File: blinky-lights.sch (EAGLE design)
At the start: 20 parts, among them Q1 N3, U1 555, U2 A2678EAT

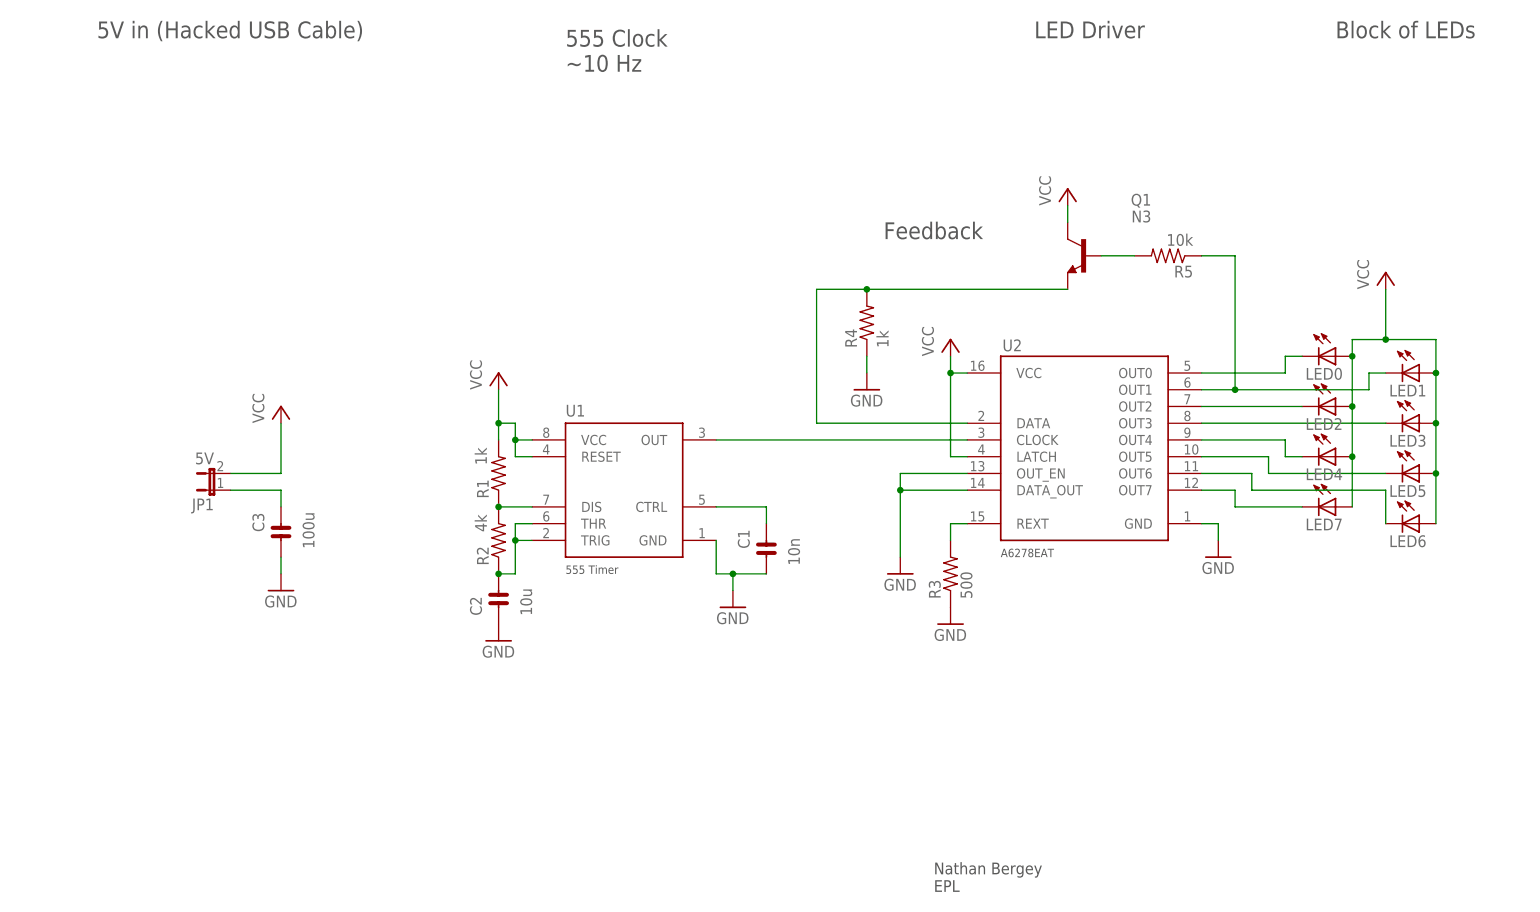
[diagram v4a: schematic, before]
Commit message: replaced transistor with a fet
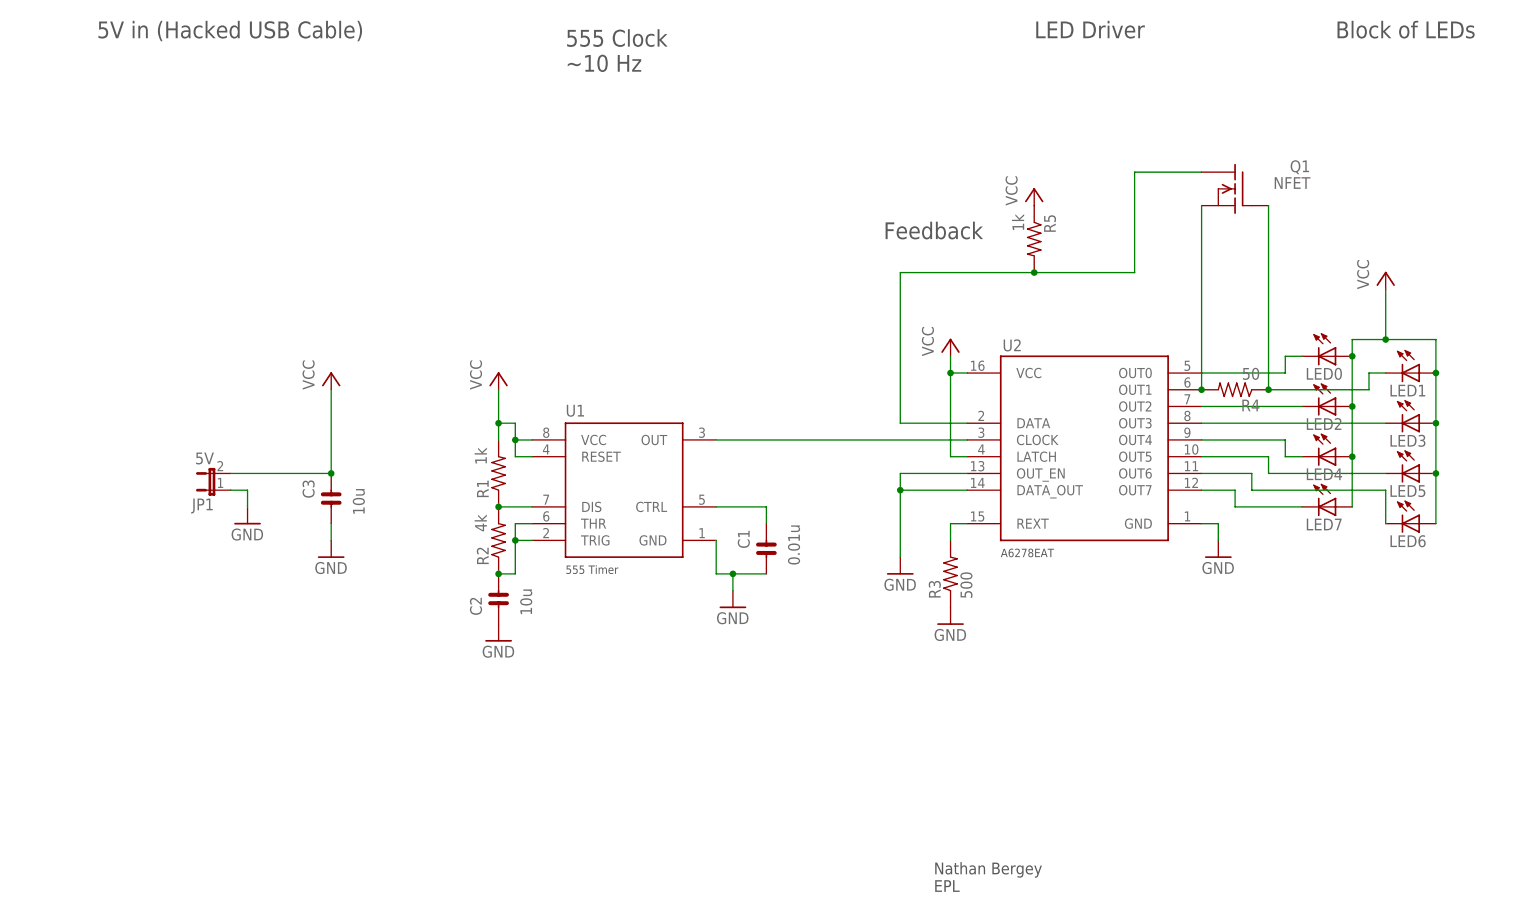
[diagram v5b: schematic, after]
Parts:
- C1: value 10n -> 0.01u
- C3: value 100u -> 10u
- LED0, LED1, LED2, LED3, LED4, LED5, LED6, LED7: device led:LED5MM -> led:LED3MM
- Q1: value N3 -> NFET; device blinky-lights:N3 -> blinky-lights:NFET
- R4: value 1k -> 50
- R5: value 10k -> 1k
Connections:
- removed net DATA: Q1.E, R4.2, U2.DATA
- removed net N$12: Q1.B, R5.2
- removed net N$13: C3.A, JP1.1
- new net N$5: Q1.S, R4.2, U2.OUT1
- net FEEDBACK: now also Q1.D, Q1.G, R4.1, R5.2, U2.DATA; no longer R5.1, U2.OUT1
- net GND: now also JP1.1; no longer R4.1
- net VCC: now also C3.A, R5.1; no longer Q1.C
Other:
- moved on the sheet: C3, Q1, R4, R5
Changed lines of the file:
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@@
 <part name="U1" library="blinky-lights" deviceset="555" device=""/>
 <part name="U2" library="blinky-lights" deviceset="A2678EAT" device=""/>
-<part name="LED0" library="led" deviceset="LED" device="5MM"/>
-<part name="LED2" library="led" deviceset="LED" device="5MM"/>
-<part name="LED4" library="led" deviceset="LED" device="5MM"/>
-<part name="LED7" library="led" deviceset="LED" device="5MM"/>
-<part name="LED1" library="led" deviceset="LED" device="5MM"/>
-<part name="LED3" library="led" deviceset="LED" device="5MM"/>
-<part name="LED5" library="led" deviceset="LED" device="5MM"/>
-<part name="LED6" library="led" deviceset="LED" device="5MM"/>
+<part name="LED0" library="led" deviceset="LED" device="3MM"/>
+<part name="LED2" library="led" deviceset="LED" device="3MM"/>
+<part name="LED4" library="led" deviceset="LED" device="3MM"/>
+<part name="LED7" library="led" deviceset="LED" device="3MM"/>
+<part name="LED1" library="led" deviceset="LED" device="3MM"/>
+<part name="LED3" library="led" deviceset="LED" device="3MM"/>
+<part name="LED5" library="led" deviceset="LED" device="3MM"/>
+<part name="LED6" library="led" deviceset="LED" device="3MM"/>
 <part name="P+1" library="supply1" deviceset="VCC" device=""/>
 <part name="P+2" library="supply1" deviceset="VCC" device=""/>
@@
 <part name="FRAME1" library="frames" deviceset="LETTER_L" device="" value="0.1"/>
 <part name="JP1" library="jumper" deviceset="JP1E" device="" value="5V"/>
-<part name="C1" library="blinky-lights" deviceset="CAP" device="" value="10n"/>
+<part name="C1" library="blinky-lights" deviceset="CAP" device="" value="0.01u"/>
 <part name="C2" library="blinky-lights" deviceset="CAP" device="" value="10u"/>
 <part name="GND6" library="supply1" deviceset="GND" device=""/>
 <part name="GND2" library="supply1" deviceset="GND" device=""/>
-<part name="Q1" library="blinky-lights" deviceset="N3*" device=""/>
-<part name="R4" library="rcl" deviceset="R-US_" device="VMTB60" value="1k"/>
-<part name="GND7" library="supply1" deviceset="GND" device=""/>
+<part name="C3" library="blinky-lights" deviceset="CAP" device="" value="10u"/>
+<part name="Q1" library="blinky-lights" deviceset="NFET" device=""/>
+<part name="GND8" library="supply1" deviceset="GND" device=""/>
+<part name="R4" library="rcl" deviceset="R-US_" device="VMTB60" value="50"/>
+<part name="R5" library="rcl" deviceset="R-US_" device="VMTB60" value="1k"/>
 <part name="P+5" library="supply1" deviceset="VCC" device=""/>
-<part name="R5" library="rcl" deviceset="R-US_" device="VMTB60" value="10k"/>
-<part name="C3" library="blinky-lights" deviceset="CAP" device="" value="100u"/>
 </parts>
 <sheets>
@@
 <instance part="P+2" gate="VCC" x="152.4" y="111.76"/>
 <instance part="P+3" gate="VCC" x="83.82" y="106.68"/>
-<instance part="P+4" gate="VCC" x="50.8" y="101.6"/>
+<instance part="P+4" gate="VCC" x="58.42" y="106.68"/>
 <instance part="GND1" gate="1" x="193.04" y="78.74"/>
-<instance part="GND3" gate="1" x="50.8" y="73.66"/>
+<instance part="GND3" gate="1" x="45.72" y="83.82"/>
 <instance part="R3" gate="G$1" x="152.4" y="76.2" rot="R90"/>
 <instance part="R1" gate="G$1" x="83.82" y="91.44" smashed="yes" rot="R90">
@@
 <instance part="GND6" gate="1" x="83.82" y="66.04"/>
 <instance part="GND2" gate="1" x="119.38" y="71.12"/>
-<instance part="Q1" gate="G$1" x="172.72" y="124.46" rot="MR0"/>
-<instance part="R4" gate="G$1" x="139.7" y="114.3" rot="R90"/>
-<instance part="GND7" gate="1" x="139.7" y="104.14"/>
-<instance part="P+5" gate="VCC" x="170.18" y="134.62"/>
-<instance part="R5" gate="G$1" x="185.42" y="124.46" rot="R180"/>
-<instance part="C3" gate="G$1" x="50.8" y="81.28" smashed="yes">
-<attribute name="NAME" x="48.26" y="82.55" size="1.778" layer="95" rot="R90"/>
-<attribute name="VALUE" x="55.88" y="80.01" size="1.778" layer="96" rot="R90"/>
-</instance>
+<instance part="C3" gate="G$1" x="58.42" y="86.36" smashed="yes">
+<attribute name="NAME" x="55.88" y="87.63" size="1.778" layer="95" rot="R90"/>
+<attribute name="VALUE" x="63.5" y="85.09" size="1.778" layer="96" rot="R90"/>
+</instance>
+<instance part="Q1" gate="G$1" x="195.58" y="134.62" rot="MR0"/>
+<instance part="GND8" gate="1" x="58.42" y="78.74"/>
+<instance part="R4" gate="G$1" x="195.58" y="104.14" rot="R180"/>
+<instance part="R5" gate="G$1" x="165.1" y="127" rot="R270"/>
+<instance part="P+5" gate="VCC" x="165.1" y="134.62"/>
 </instances>
 <busses>
@@
 <wire x1="218.44" y1="106.68" x2="215.9" y2="106.68" width="0.1524" layer="91"/>
 <wire x1="215.9" y1="106.68" x2="215.9" y2="104.14" width="0.1524" layer="91"/>
-<pinref part="U2" gate="G$1" pin="OUT1"/>
-<wire x1="215.9" y1="104.14" x2="195.58" y2="104.14" width="0.1524" layer="91"/>
-<wire x1="195.58" y1="104.14" x2="190.5" y2="104.14" width="0.1524" layer="91"/>
-<wire x1="195.58" y1="104.14" x2="195.58" y2="124.46" width="0.1524" layer="91"/>
-<junction x="195.58" y="104.14"/>
-<pinref part="R5" gate="G$1" pin="1"/>
-<wire x1="190.5" y1="124.46" x2="195.58" y2="124.46" width="0.1524" layer="91"/>
+<pinref part="R4" gate="G$1" pin="1"/>
+<wire x1="200.66" y1="104.14" x2="215.9" y2="104.14" width="0.1524" layer="91"/>
+<wire x1="200.66" y1="104.14" x2="200.66" y2="132.08" width="0.1524" layer="91"/>
+<junction x="200.66" y="104.14"/>
+<pinref part="Q1" gate="G$1" pin="G"/>
+</segment>
+<segment>
+<pinref part="U2" gate="G$1" pin="DATA"/>
+<wire x1="154.94" y1="99.06" x2="144.78" y2="99.06" width="0.1524" layer="91"/>
+<wire x1="144.78" y1="99.06" x2="144.78" y2="121.92" width="0.1524" layer="91"/>
+<pinref part="R5" gate="G$1" pin="2"/>
+<wire x1="144.78" y1="121.92" x2="165.1" y2="121.92" width="0.1524" layer="91"/>
+<wire x1="165.1" y1="121.92" x2="180.34" y2="121.92" width="0.1524" layer="91"/>
+<wire x1="180.34" y1="121.92" x2="180.34" y2="137.16" width="0.1524" layer="91"/>
+<junction x="165.1" y="121.92"/>
+<pinref part="Q1" gate="G$1" pin="D"/>
+<wire x1="180.34" y1="137.16" x2="190.5" y2="137.16" width="0.1524" layer="91"/>
 </segment>
 </net>
@@
 </segment>
 <segment>
+<pinref part="C3" gate="G$1" pin="A"/>
+<pinref part="P+4" gate="VCC" pin="VCC"/>
+<wire x1="58.42" y1="91.44" x2="58.42" y2="104.14" width="0.1524" layer="91"/>
 <pinref part="JP1" gate="A" pin="2"/>
-<pinref part="P+4" gate="VCC" pin="VCC"/>
-<wire x1="43.18" y1="91.44" x2="50.8" y2="91.44" width="0.1524" layer="91"/>
-<wire x1="50.8" y1="91.44" x2="50.8" y2="99.06" width="0.1524" layer="91"/>
-</segment>
-<segment>
-<pinref part="Q1" gate="G$1" pin="C"/>
+<wire x1="43.18" y1="91.44" x2="58.42" y2="91.44" width="0.1524" layer="91"/>
+<junction x="58.42" y="91.44"/>
+</segment>
+<segment>
+<pinref part="R5" gate="G$1" pin="1"/>
 <pinref part="P+5" gate="VCC" pin="VCC"/>
-<wire x1="170.18" y1="129.54" x2="170.18" y2="132.08" width="0.1524" layer="91"/>
 </segment>
 </net>
@@
 </segment>
 <segment>
-<pinref part="R4" gate="G$1" pin="1"/>
-<pinref part="GND7" gate="1" pin="GND"/>
-<wire x1="139.7" y1="106.68" x2="139.7" y2="109.22" width="0.1524" layer="91"/>
+<pinref part="JP1" gate="A" pin="1"/>
+<pinref part="GND3" gate="1" pin="GND"/>
+<wire x1="43.18" y1="88.9" x2="45.72" y2="88.9" width="0.1524" layer="91"/>
+<wire x1="45.72" y1="88.9" x2="45.72" y2="86.36" width="0.1524" layer="91"/>
 </segment>
 <segment>
 <pinref part="C3" gate="G$1" pin="C"/>
-<pinref part="GND3" gate="1" pin="GND"/>
-<wire x1="50.8" y1="78.74" x2="50.8" y2="76.2" width="0.1524" layer="91"/>
+<pinref part="GND8" gate="1" pin="GND"/>
+<wire x1="58.42" y1="81.28" x2="58.42" y2="83.82" width="0.1524" layer="91"/>
 </segment>
 </net>
@@
 </segment>
 </net>
-<net name="DATA" class="0">
-<segment>
-<wire x1="139.7" y1="119.38" x2="132.08" y2="119.38" width="0.1524" layer="91"/>
-<wire x1="132.08" y1="119.38" x2="132.08" y2="99.06" width="0.1524" layer="91"/>
-<pinref part="U2" gate="G$1" pin="DATA"/>
-<wire x1="132.08" y1="99.06" x2="154.94" y2="99.06" width="0.1524" layer="91"/>
+<net name="N$5" class="0">
+<segment>
+<pinref part="U2" gate="G$1" pin="OUT1"/>
 <pinref part="R4" gate="G$1" pin="2"/>
-<pinref part="Q1" gate="G$1" pin="E"/>
-<wire x1="170.18" y1="119.38" x2="139.7" y2="119.38" width="0.1524" layer="91"/>
-<junction x="139.7" y="119.38"/>
-</segment>
-</net>
-<net name="N$12" class="0">
-<segment>
-<pinref part="R5" gate="G$1" pin="2"/>
-<pinref part="Q1" gate="G$1" pin="B"/>
-<wire x1="180.34" y1="124.46" x2="175.26" y2="124.46" width="0.1524" layer="91"/>
-</segment>
-</net>
-<net name="N$13" class="0">
-<segment>
-<pinref part="JP1" gate="A" pin="1"/>
-<wire x1="43.18" y1="88.9" x2="50.8" y2="88.9" width="0.1524" layer="91"/>
-<pinref part="C3" gate="G$1" pin="A"/>
-<wire x1="50.8" y1="88.9" x2="50.8" y2="86.36" width="0.1524" layer="91"/>
-</segment>
-</net>
+<pinref part="Q1" gate="G$1" pin="S"/>
+<wire x1="190.5" y1="132.08" x2="190.5" y2="104.14" width="0.1524" layer="91"/>
+<junction x="190.5" y="104.14"/>
+</segment>
+</net>

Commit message: board layout
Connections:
- new net SENSE: LED1.C, Q1.G, R4.1
- net FEEDBACK: no longer LED1.C, Q1.G, R4.1
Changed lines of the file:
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@@
 <net name="FEEDBACK" class="0">
-<segment>
-<pinref part="LED1" gate="G$1" pin="C"/>
-<wire x1="218.44" y1="106.68" x2="215.9" y2="106.68" width="0.1524" layer="91"/>
-<wire x1="215.9" y1="106.68" x2="215.9" y2="104.14" width="0.1524" layer="91"/>
-<pinref part="R4" gate="G$1" pin="1"/>
-<wire x1="200.66" y1="104.14" x2="215.9" y2="104.14" width="0.1524" layer="91"/>
-<wire x1="200.66" y1="104.14" x2="200.66" y2="132.08" width="0.1524" layer="91"/>
-<junction x="200.66" y="104.14"/>
-<pinref part="Q1" gate="G$1" pin="G"/>
-</segment>
 <segment>
 <pinref part="U2" gate="G$1" pin="DATA"/>
@@
 </segment>
 </net>
+<net name="SENSE" class="0">
+<segment>
+<pinref part="LED1" gate="G$1" pin="C"/>
+<wire x1="218.44" y1="106.68" x2="215.9" y2="106.68" width="0.1524" layer="91"/>
+<wire x1="215.9" y1="106.68" x2="215.9" y2="104.14" width="0.1524" layer="91"/>
+<pinref part="R4" gate="G$1" pin="1"/>
+<wire x1="200.66" y1="104.14" x2="215.9" y2="104.14" width="0.1524" layer="91"/>
+<wire x1="200.66" y1="104.14" x2="200.66" y2="132.08" width="0.1524" layer="91"/>
+<junction x="200.66" y="104.14"/>
+<pinref part="Q1" gate="G$1" pin="G"/>
+</segment>
+</net>
 </nets>
 </sheet>
 </sheets>
+<errors>
+</errors>
 </schematic>
 </drawing>

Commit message: schematic and board clean up
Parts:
- R4: value 50 -> 10
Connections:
- net SENSE: no longer Q1.G
- net VCC: now also Q1.G
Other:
- note added: "555 In Astable Mode ~10 Hz"
- note added: "LED Driver/Shift Register"
- note removed: "555 Clock ~10 Hz"
- note removed: "Feedback"
- note removed: "LED Driver"
- moved on the sheet: C1, C2, C3, JP1, LED0, LED1, LED2, LED3, LED4, LED5, LED6, LED7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

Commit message: board clean up, got rid of last airwire
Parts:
- LED0, LED1, LED2, LED3, LED4, LED5, LED6, LED7: value (none) -> LED3MM; device led:LED3MM -> blinky-lights:LED3MM
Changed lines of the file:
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@@
 <part name="U1" library="blinky-lights" deviceset="555" device=""/>
 <part name="U2" library="blinky-lights" deviceset="A2678EAT" device=""/>
-<part name="LED0" library="led" deviceset="LED" device="3MM"/>
-<part name="LED2" library="led" deviceset="LED" device="3MM"/>
-<part name="LED4" library="led" deviceset="LED" device="3MM"/>
-<part name="LED7" library="led" deviceset="LED" device="3MM"/>
-<part name="LED1" library="led" deviceset="LED" device="3MM"/>
-<part name="LED3" library="led" deviceset="LED" device="3MM"/>
-<part name="LED5" library="led" deviceset="LED" device="3MM"/>
-<part name="LED6" library="led" deviceset="LED" device="3MM"/>
+<part name="LED0" library="blinky-lights" deviceset="LED3MM" device=""/>
+<part name="LED2" library="blinky-lights" deviceset="LED3MM" device=""/>
+<part name="LED4" library="blinky-lights" deviceset="LED3MM" device=""/>
+<part name="LED7" library="blinky-lights" deviceset="LED3MM" device=""/>
+<part name="LED1" library="blinky-lights" deviceset="LED3MM" device=""/>
+<part name="LED3" library="blinky-lights" deviceset="LED3MM" device=""/>
+<part name="LED5" library="blinky-lights" deviceset="LED3MM" device=""/>
+<part name="LED6" library="blinky-lights" deviceset="LED3MM" device=""/>
 <part name="P+1" library="supply1" deviceset="VCC" device=""/>
 <part name="P+2" library="supply1" deviceset="VCC" device=""/>
@@
 <instance part="U1" gate="G$1" x="88.9" y="93.98"/>
 <instance part="U2" gate="G$1" x="162.56" y="99.06"/>
-<instance part="LED0" gate="G$1" x="210.82" y="114.3" rot="R270"/>
-<instance part="LED2" gate="G$1" x="210.82" y="106.68" rot="R270"/>
-<instance part="LED4" gate="G$1" x="210.82" y="99.06" rot="R270"/>
-<instance part="LED7" gate="G$1" x="210.82" y="91.44" rot="R270"/>
-<instance part="LED1" gate="G$1" x="223.52" y="111.76" rot="R270"/>
-<instance part="LED3" gate="G$1" x="223.52" y="104.14" rot="R270"/>
-<instance part="LED5" gate="G$1" x="223.52" y="96.52" rot="R270"/>
-<instance part="LED6" gate="G$1" x="223.52" y="88.9" rot="R270"/>
+<instance part="LED0" gate="G$1" x="210.82" y="114.3" smashed="yes" rot="R270">
+<attribute name="NAME" x="206.248" y="110.744" size="1.778" layer="95"/>
+</instance>
+<instance part="LED2" gate="G$1" x="210.82" y="106.68" smashed="yes" rot="R270">
+<attribute name="NAME" x="206.248" y="103.124" size="1.778" layer="95"/>
+</instance>
+<instance part="LED4" gate="G$1" x="210.82" y="99.06" smashed="yes" rot="R270">
+<attribute name="NAME" x="206.248" y="95.504" size="1.778" layer="95"/>
+</instance>
+<instance part="LED7" gate="G$1" x="210.82" y="91.44" smashed="yes" rot="R270">
+<attribute name="NAME" x="206.248" y="87.884" size="1.778" layer="95"/>
+</instance>
+<instance part="LED1" gate="G$1" x="223.52" y="111.76" smashed="yes" rot="R270">
+<attribute name="NAME" x="218.948" y="108.204" size="1.778" layer="95"/>
+</instance>
+<instance part="LED3" gate="G$1" x="223.52" y="104.14" smashed="yes" rot="R270">
+<attribute name="NAME" x="218.948" y="100.584" size="1.778" layer="95"/>
+</instance>
+<instance part="LED5" gate="G$1" x="223.52" y="96.52" smashed="yes" rot="R270">
+<attribute name="NAME" x="218.948" y="92.964" size="1.778" layer="95"/>
+</instance>
+<instance part="LED6" gate="G$1" x="223.52" y="88.9" smashed="yes" rot="R270">
+<attribute name="NAME" x="218.948" y="85.344" size="1.778" layer="95"/>
+</instance>
 <instance part="P+1" gate="VCC" x="218.44" y="137.16"/>
 <instance part="P+2" gate="VCC" x="142.24" y="116.84"/>
